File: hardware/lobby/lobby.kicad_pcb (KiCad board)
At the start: 4 copper layers, 85 x 56 mm, 41 parts, among them J1 THD-02-R, J2 THD-20-R, J3 Micro_SD_Card_Det, J4 Conn_01x22_Female, SW1 SW_SPST, SW2 SW_SPST, U1 RT9742GGJ5, U2 M.2-keyM, U3 MYLSM00502ERPL, U4 FSUSB42MX

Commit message: cam v2
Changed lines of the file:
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@@
     (fp_line (start -1 -0.625) (end 1 -0.625) (layer "B.Fab") (width 0.1))
     (fp_line (start -0.6875 0.625) (end -1 0.3125) (layer "B.Fab") (width 0.1))
-    (pad "1" smd roundrect locked (at -0.8875 0 90) (size 1.125 1.05) (layers "B.Cu" "B.Paste" "B.Mask") (roundrect_rratio 0.238095)
+    (pad "1" smd roundrect locked (at -0.8875 0 90) (size 1.125 1.05) (layers "B.Cu" "B.Paste" "B.Mask") (roundrect_rratio 0.2380952381)
       (net 3 "/+3.3v"))
-    (pad "2" smd roundrect locked (at 0.8875 0 90) (size 1.125 1.05) (layers "B.Cu" "B.Paste" "B.Mask") (roundrect_rratio 0.238095)
+    (pad "2" smd roundrect locked (at 0.8875 0 90) (size 1.125 1.05) (layers "B.Cu" "B.Paste" "B.Mask") (roundrect_rratio 0.2380952381)
       (net 2 "GND"))
     (model "${KICAD6_3DMODEL_DIR}/Capacitor_Tantalum_SMD.3dshapes/CP_EIA-2012-15_AVX-P.wrl"
@@
     (property "Sheetfile" "./sheets/jumpers.kicad_sch")
     (property "Sheetname" "jumpers")
-    (fp_text reference "SW1" (at 8.01 -2.6 180 unlocked) (layer "B.SilkS")
+    (fp_text reference "SW1" (at 8.01 -2.6 180 unlocked) (layer "B.SilkS") hide
       (effects (font (size 1 1) (thickness 0.15)) (justify mirror))
     )
-    (fp_text value "SW_SPST" (at 8.01 -4.1 180 unlocked) (layer "B.Fab")
+    (fp_text value "SW_SPST" (at 8.01 -4.1 180 unlocked) (layer "B.Fab") hide
       (effects (font (size 1 1) (thickness 0.15)) (justify mirror))
     )
-    (fp_text user "${REFERENCE}" (at 8.01 -5.6 180 unlocked) (layer "B.Fab")
+    (fp_text user "${REFERENCE}" (at 0.5 -2.7 180 unlocked) (layer "B.Fab")
       (effects (font (size 1 1) (thickness 0.15)) (justify mirror))
     )

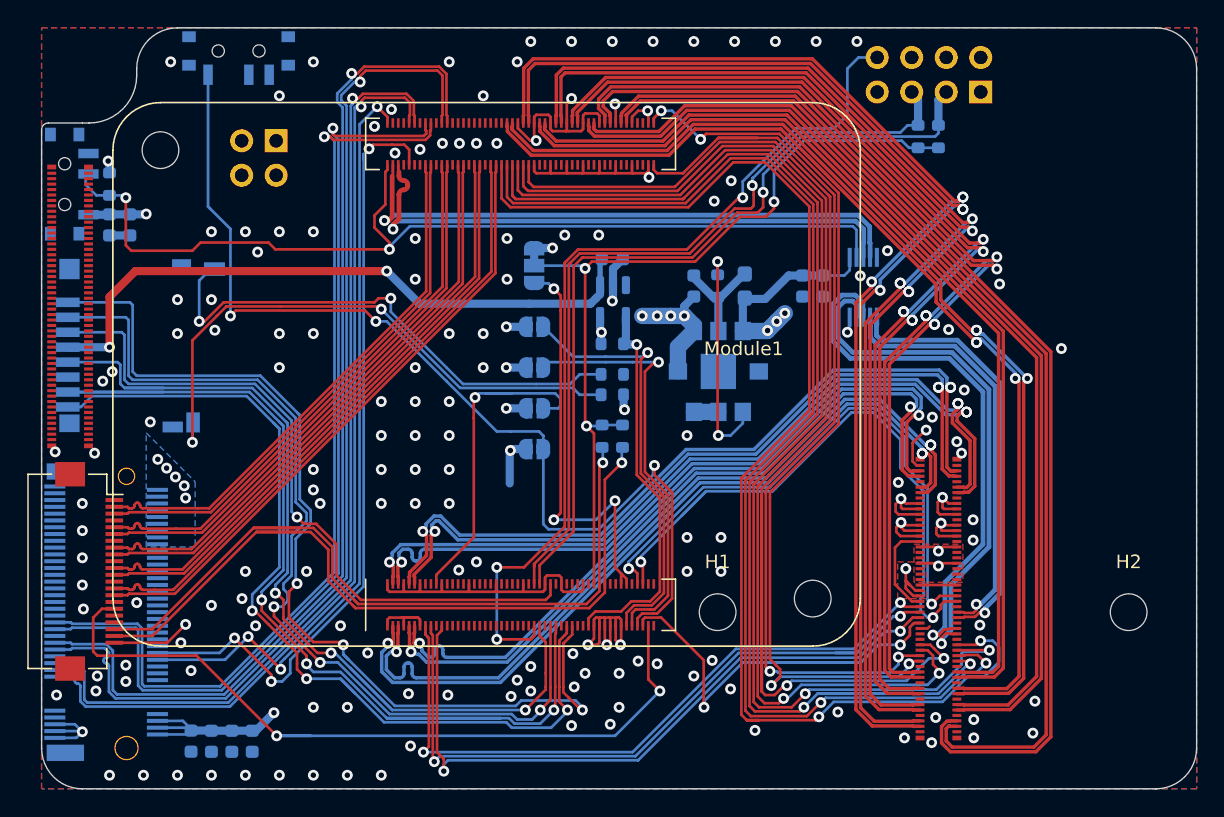
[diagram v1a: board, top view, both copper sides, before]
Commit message: change lobby hirose connectors to the DS variant
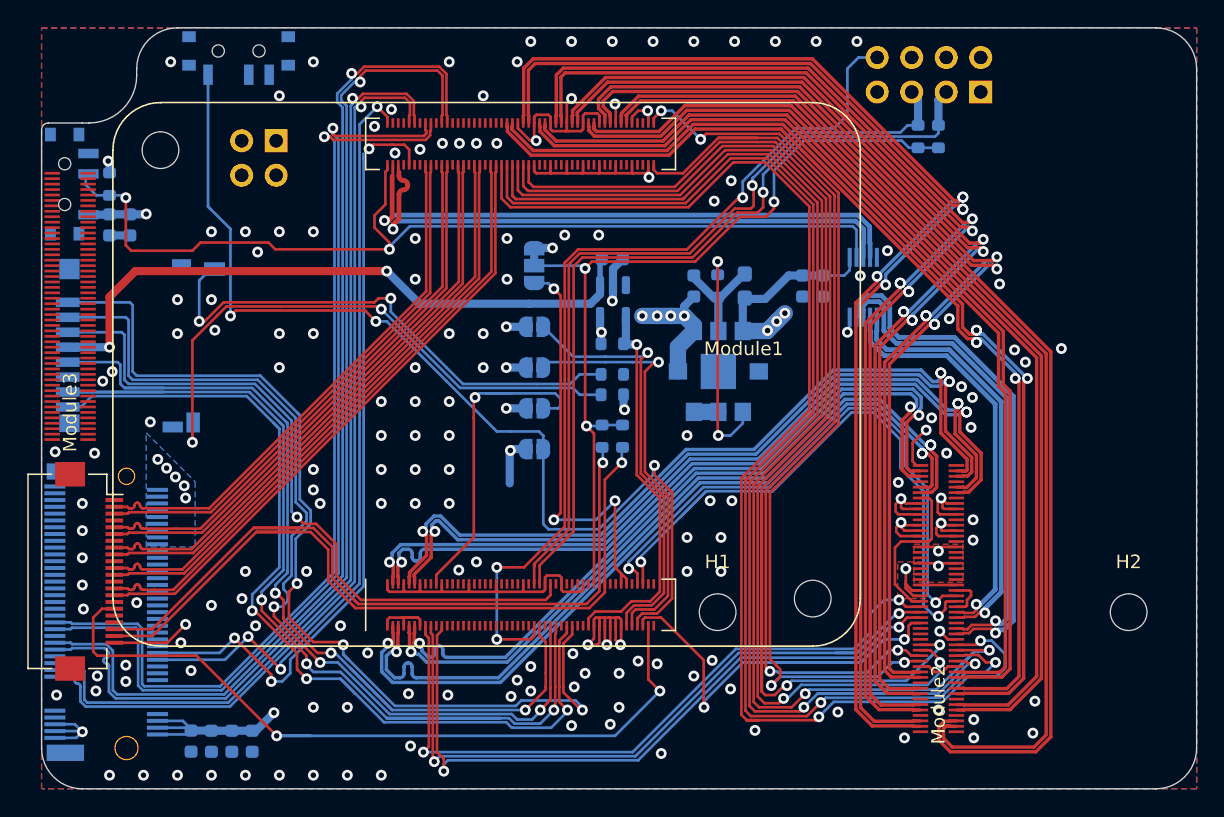
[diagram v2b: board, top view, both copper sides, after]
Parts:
- removed REF**: subluminal-logo, cm4crypto:subluminal-logo
- Module2, Module3: footprint cm4crypto:DF40C-100DP-0.4V(51) -> cm4crypto:DF40C-100DS-0.4V(51)
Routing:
- net GND: track 103.3 -> 114.8 mm, vias 160 -> 165
- net /USB2_DEV_N: track 40.7 -> 36.1 mm
- net /TRD0_P: track 56.7 -> 58.2 mm
- net /HDMI1_HOTPLUG: track 95.5 -> 97.0 mm
- net /HDMI1_SDA: track 89.8 -> 91.2 mm
- net /TRD0_N: track 57.2 -> 58.5 mm
- net /USB2_DEV_P: track 39.4 -> 38.3 mm
- net /HDMI1_CEC: track 89.0 -> 90.1 mm
- net /ETH_LEDY: track 50.8 -> 51.8 mm
- net /HDMI0_HOTPLUG: track 96.8 -> 97.7 mm
- net /HDMI1_TX0_P: track 69.9 -> 70.6 mm
- net /HDMI1_TX0_N: track 70.5 -> 71.2 mm
- net /HDMI1_SCL: track 93.9 -> 94.6 mm
- net /USB2_HOST_N: track 31.6 -> 31.0 mm
- net /USB2_HOST_P: track 31.0 -> 30.4 mm
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
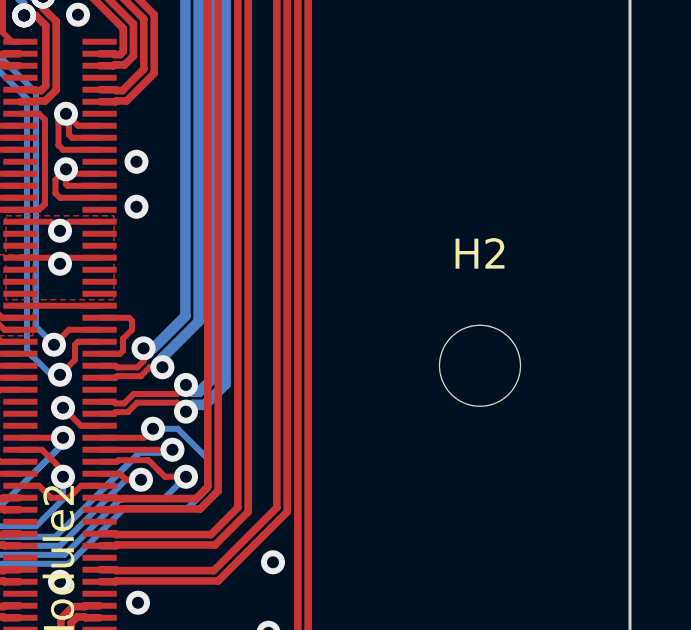
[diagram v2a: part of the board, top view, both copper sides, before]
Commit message: move m.2 adaptor mount hole
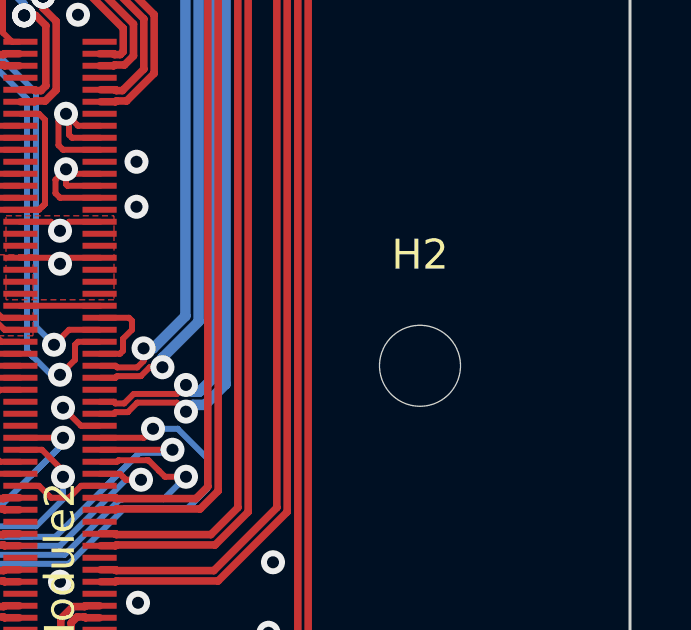
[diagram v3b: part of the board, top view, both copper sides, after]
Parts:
- moved H2 2.00 mm to (98.0, 63.0)
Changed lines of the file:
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@@
   )
   (footprint "MountingHole:MountingHole_2.7mm_M2.5" (layer "F.Cu")
-    (at 100 63)
+    (at 98 63)
     (descr "Mounting Hole 2.7mm, no annular, M2.5")
     (tags "mounting hole 2.7mm no annular m2.5")

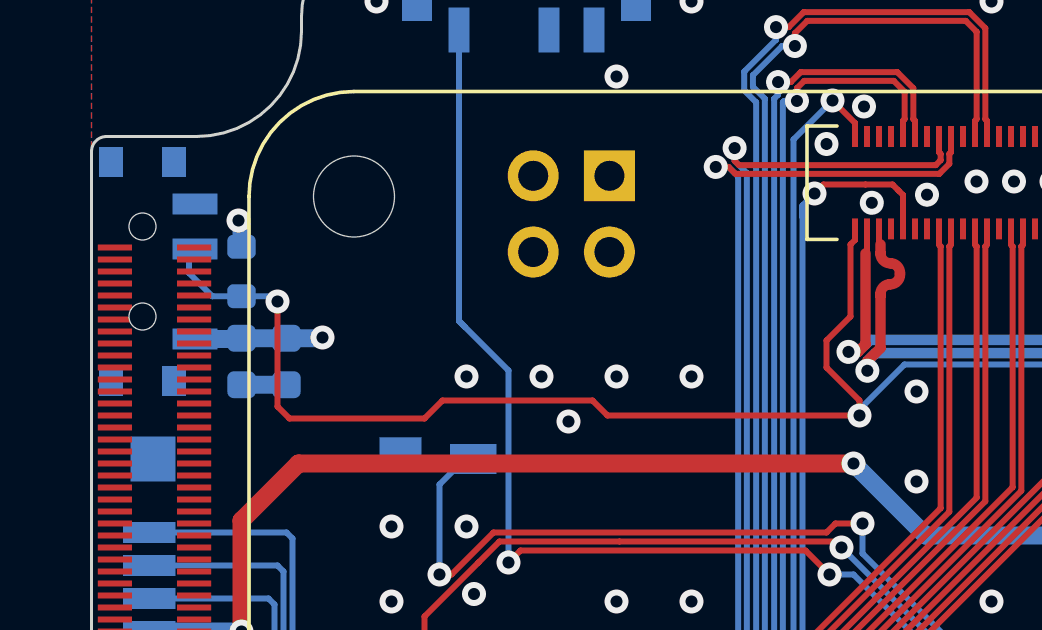
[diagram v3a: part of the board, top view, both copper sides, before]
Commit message: relabel switches
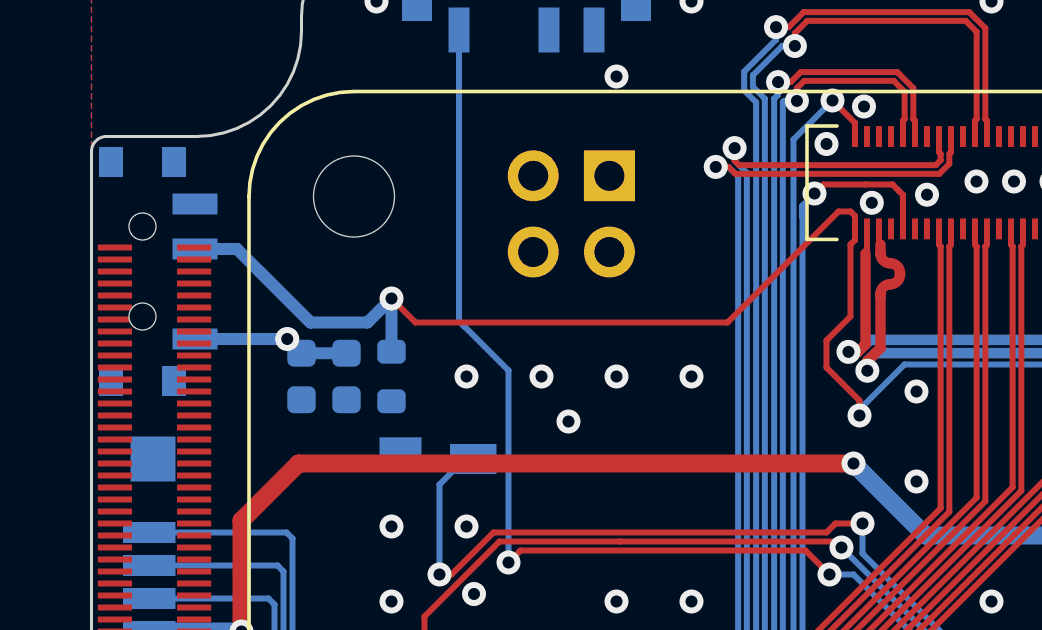
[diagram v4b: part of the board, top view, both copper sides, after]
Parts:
- moved R8 6.10 mm to (30.0, 35.0), turned to -90 degrees
- moved C2 2.06 mm to (28.5, 35.0)
- moved C3 2.06 mm to (27.0, 35.0)
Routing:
- net GND: track 114.8 -> 112.4 mm, vias 165 -> 164
- net /USBOTG_ID: track 72.1 -> 74.3 mm
- net /+3.3v: track 240.2 -> 241.6 mm
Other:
- board text added: "A"
- board text added: "C"
- board text added: "MSD"
- board text added: "NOM"
- board text added: "USB"
- board text removed: "DEV"
- board text removed: "INTERNAL"
- board text removed: "OTG"
- board text removed: "RPIBOOT"
- board text removed: "USB-C"

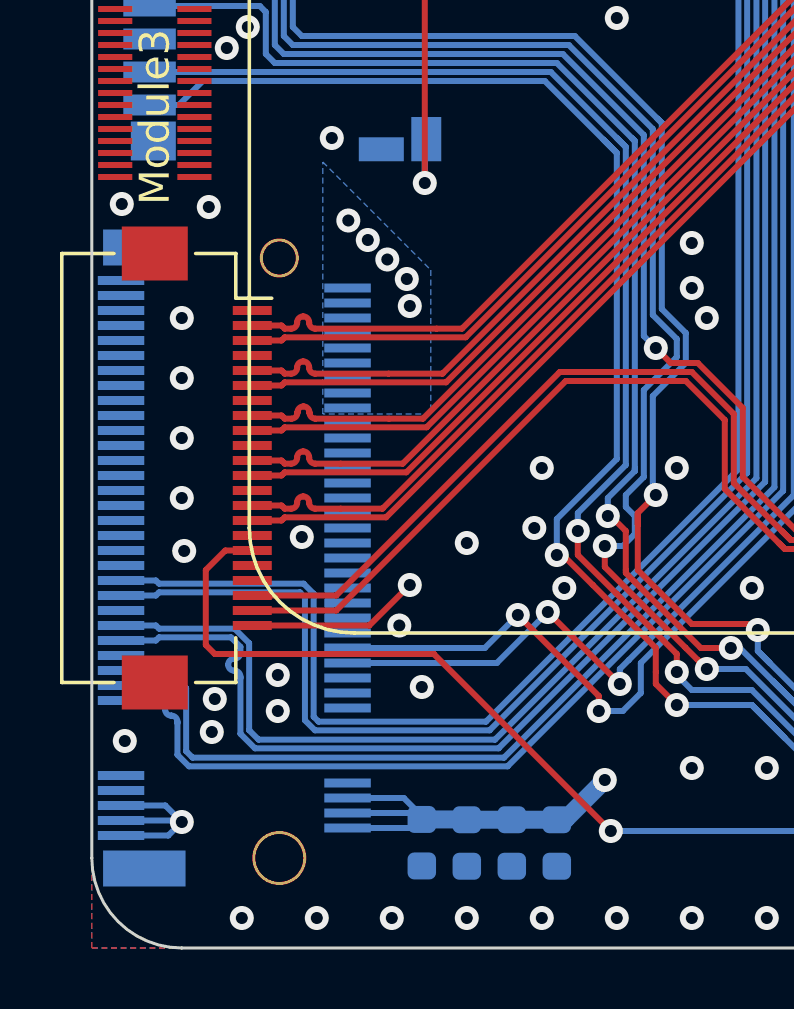
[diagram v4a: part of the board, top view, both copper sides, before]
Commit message: update camera connector footprint
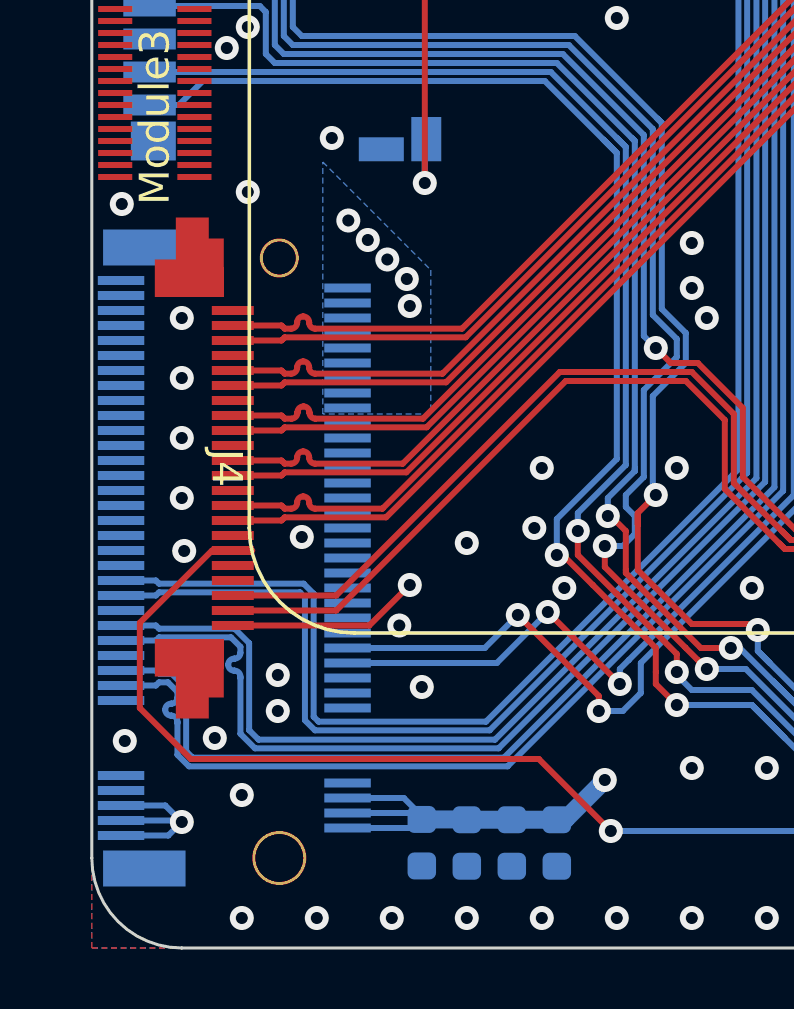
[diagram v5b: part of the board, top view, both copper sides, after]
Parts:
- J4: footprint Connector_FFC-FPC:Hirose_FH12-22S-0.5SH_1x22-1MP_P0.50mm_Horizontal -> cm4crypto:SFV22R-2STE1HLF
- moved J4 0.50 mm to (24.0, 60.0)
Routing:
- net /CAM_GPIO: track 57.7 -> 62.5 mm
- net /CAM1_D2_N: track 44.2 -> 44.9 mm
- net /SCL0: track 57.5 -> 58.1 mm
- net /CAM1_D2_P: track 44.3 -> 44.9 mm
- net /CAM1_D1_N: track 41.0 -> 41.7 mm
- net /CAM1_D0_P: track 39.4 -> 40.1 mm
- net /CAM1_D0_N: track 39.4 -> 40.0 mm
- net /CAM1_C_P: track 42.7 -> 43.3 mm
- net /+3.3v: track 241.6 -> 242.3 mm
- net /SDA0: track 58.2 -> 58.9 mm
- net /CAM1_D3_P: track 45.9 -> 46.5 mm
- net /CAM1_D3_N: track 45.8 -> 46.5 mm
- net /CAM1_D1_P: track 41.0 -> 41.7 mm
- net /CAM1_C_N: track 42.6 -> 43.3 mm
